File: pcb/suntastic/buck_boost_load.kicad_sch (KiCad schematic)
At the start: 2 parts, among them J5 Vin_TO_buck_boost, J6 Vout_FROM_buck_boost

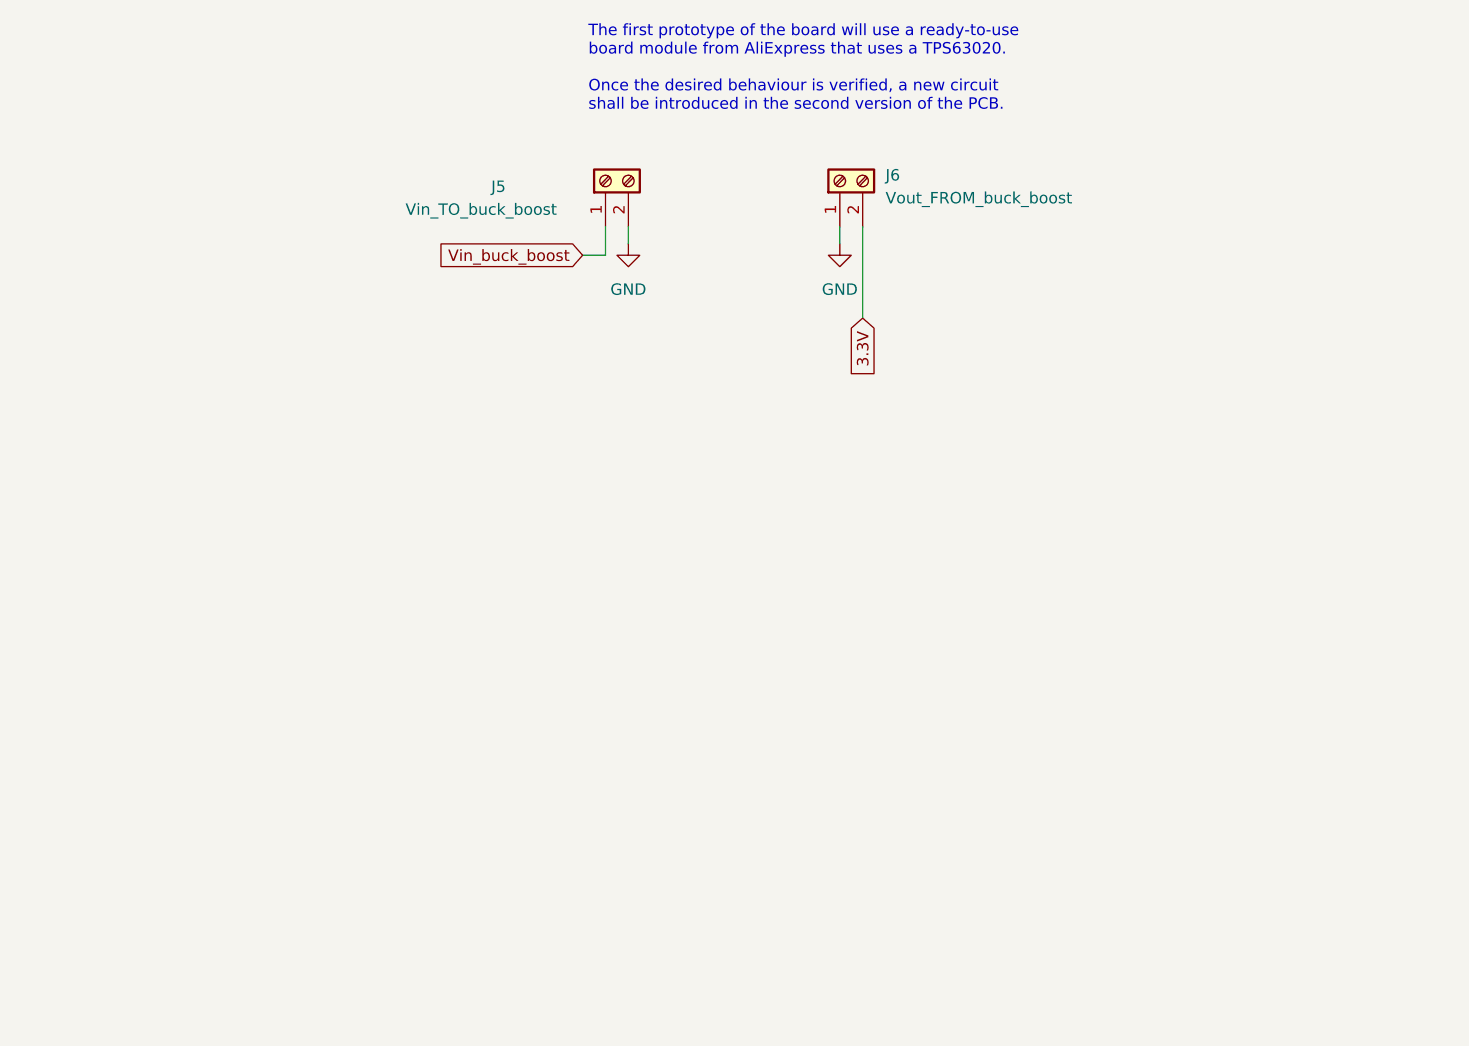
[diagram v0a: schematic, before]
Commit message: Add two alternatives to obtain 3.3V for the SX chip
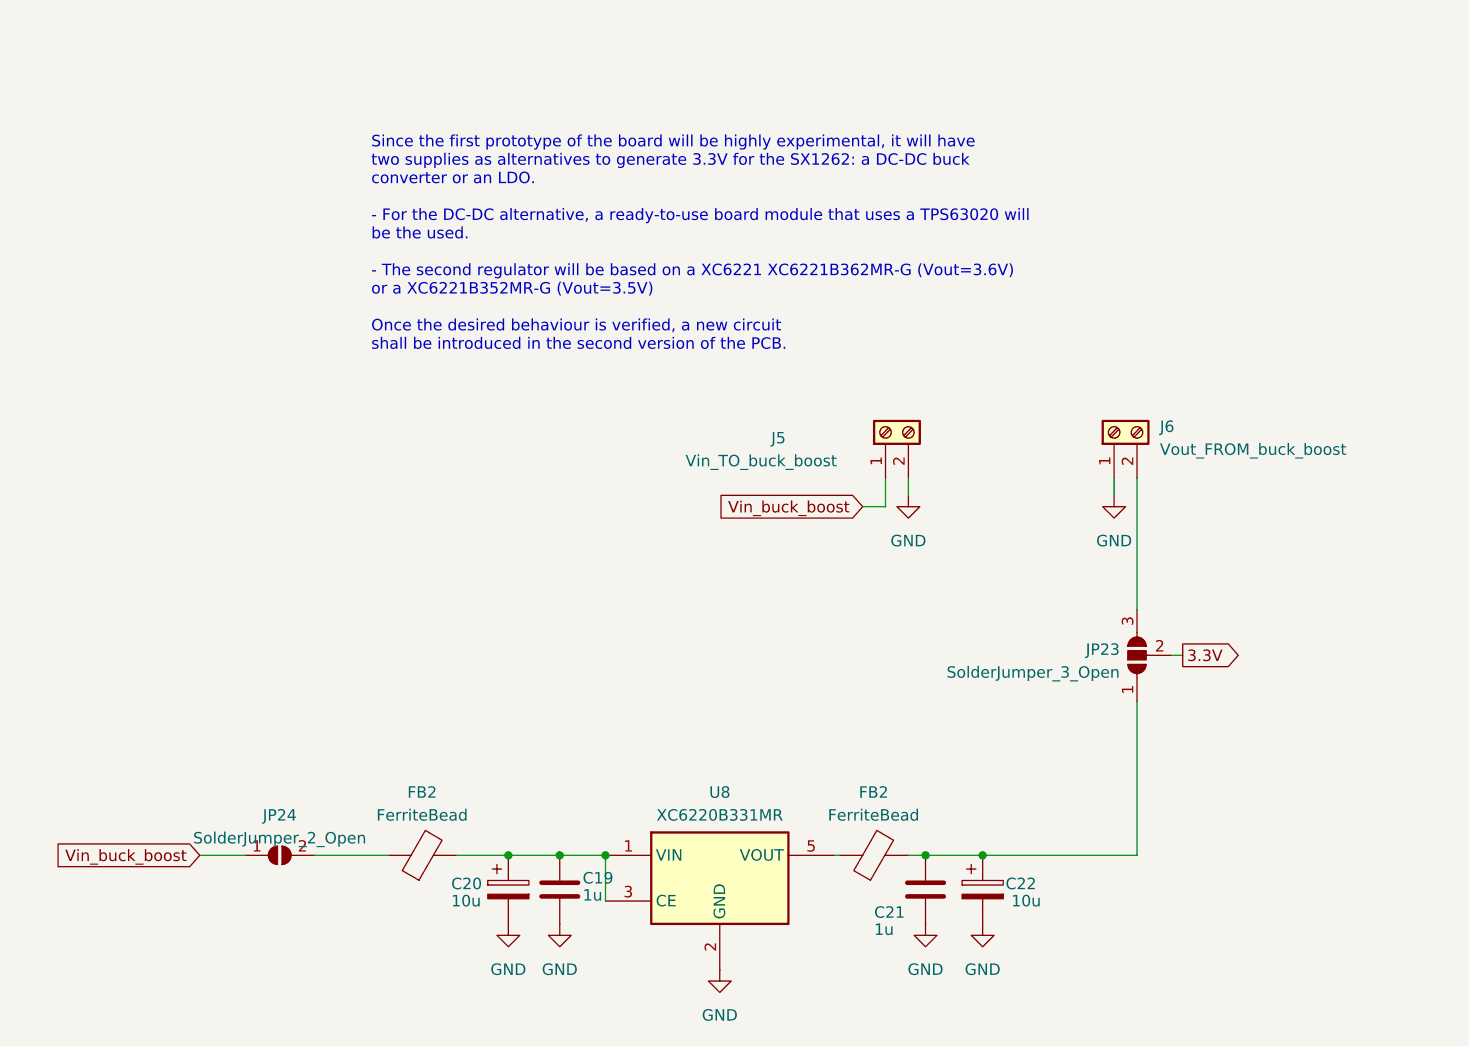
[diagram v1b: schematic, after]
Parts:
- added C19, C21: 1u, symbol Device:C
- added C20, C22: 10u, symbol Device:C_Polarized
- added FB2 (x2): FerriteBead, symbol Device:FerriteBead
- added JP23: SolderJumper_3_Open, symbol Jumper:SolderJumper_3_Open
- added JP24: SolderJumper_2_Open, symbol Jumper:SolderJumper_2_Open
- added U8: XC6220B331MR, Package_TO_SOT_SMD:SOT-23-5_HandSoldering, symbol Regulator_Linear:XC6220B331MR
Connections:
- net 3.3V: now also JP23.2 (C); no longer J6.2 (Pin_2)
- net GND: now also C19.2, C20.2, C21.2, C22.2, U8.2 (GND)
- net Vin_buck_boost: now also JP24.1 (A)
- new net: FB2.1, U8.5 (VOUT)
- new net: C21.1, C22.1, FB2.2, JP23.1 (A)
- new net: C19.1, C20.1, FB2.2, U8.1 (VIN), U8.3 (CE)
- new net: J6.2 (Pin_2), JP23.3 (B)
- new net: FB2.1, JP24.2 (B)
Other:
- note added: "Since the first prototype of the board will be highly experimental, it will have two supplies as alternatives to generate 3.3V for the SX1262: a DC-DC buck converter or an LDO. - For the DC-DC alternative, a ready-to-use board module that uses a TPS63020 will be the used. - The second regulator will be based on a XC6221 XC6221B362MR-G (Vout=3.6V) or a XC6221B352MR-G (Vout=3.5V) Once the desired b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"
- note removed: "The first prototype of the board will use a ready-to-use board module from AliExpress that uses a TPS63020. Once the desired behaviour is verified, a new circuit shall be introduced in the second version of the PCB."
- moved on the sheet: J5, J6

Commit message: Update footprints
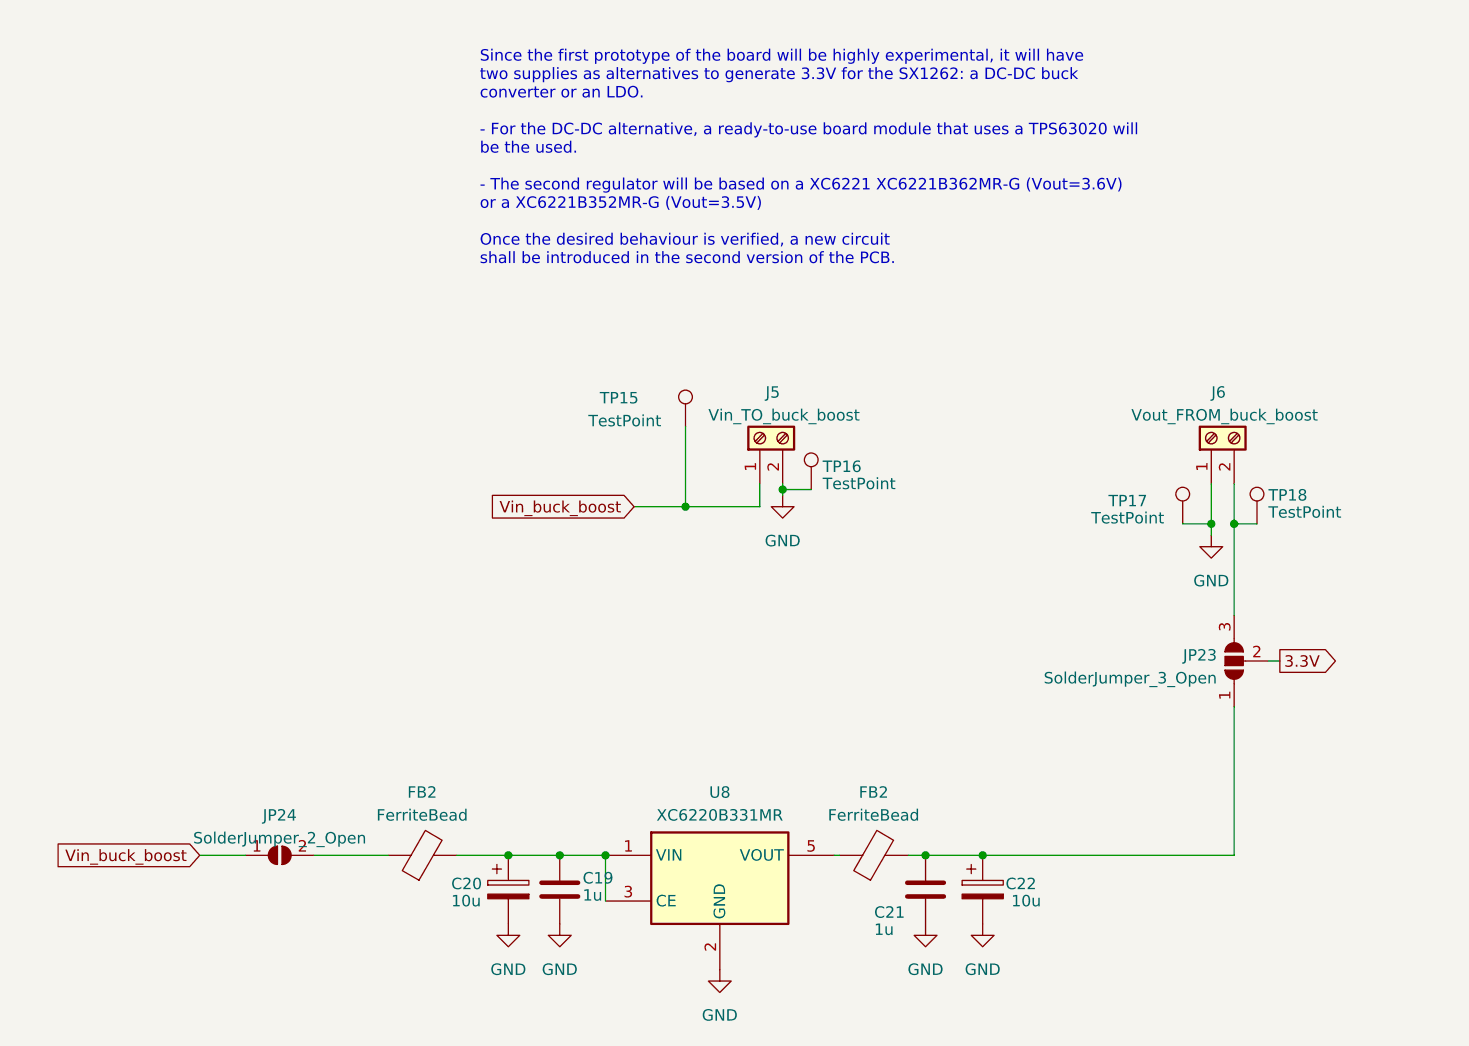
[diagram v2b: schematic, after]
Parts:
- added TP15, TP16, TP17, TP18: TestPoint, TestPoint:TestPoint_THTPad_4.0x4.0mm_Drill2.0mm, symbol Connector:TestPoint
- JP23: footprint (none) -> Jumper:SolderJumper-3_P1.3mm_Open_RoundedPad1.0x1.5mm_NumberLabels
- JP24: footprint (none) -> Jumper:SolderJumper-2_P1.3mm_Open_RoundedPad1.0x1.5mm
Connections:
- net GND: now also TP16.1, TP17.1
- net Vin_buck_boost: now also TP15.1
- net at J6.2 (Pin_2), JP23.3 (B): now also TP18.1
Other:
- moved on the sheet: J5, J6, JP23

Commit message: Update more footprints and start with PCB
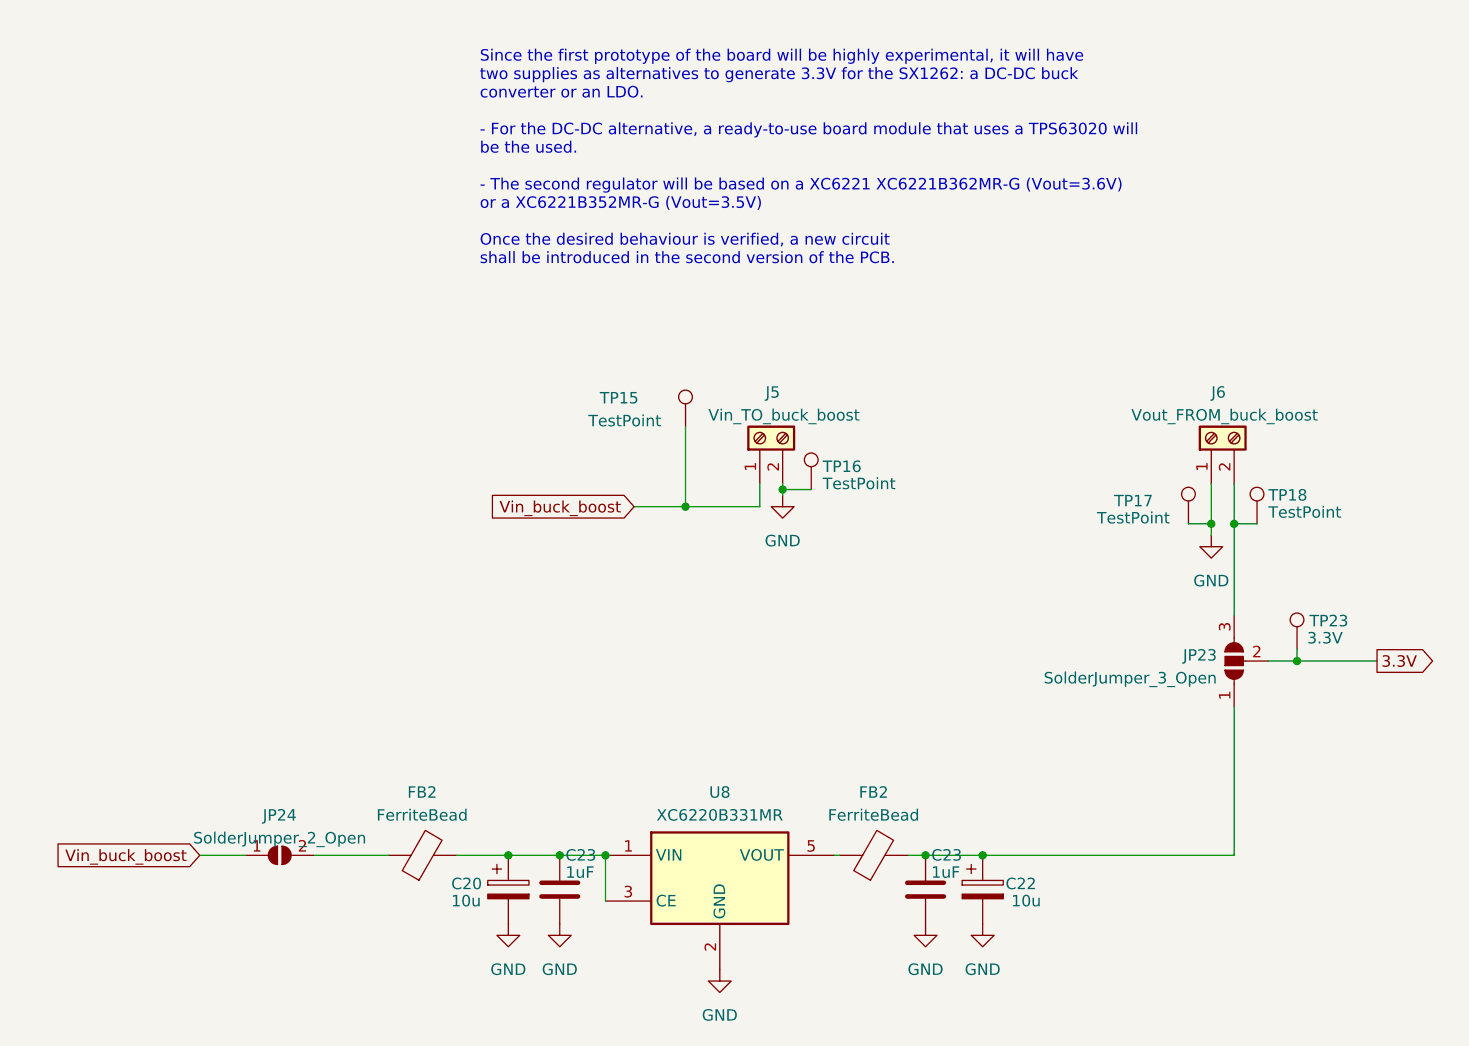
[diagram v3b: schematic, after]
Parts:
- removed C19, C21: 1u, symbol Device:C
- added C23 (x2): 1uF, Capacitor_SMD:C_0603_1608Metric_Pad1.08x0.95mm_HandSolder, symbol Device:C
- added TP23: 3.3V, TestPoint:TestPoint_Bridge_Pitch5.08mm_Drill1.3mm, symbol Connector:TestPoint
- C20, C22: footprint (none) -> Capacitor_SMD:CP_Elec_4x4.5
- FB2: footprint (none) -> Inductor_SMD:L_0603_1608Metric_Pad1.05x0.95mm_HandSolder
- J5, J6: footprint (none) -> TerminalBlock:TerminalBlock_bornier-2_P5.08mm
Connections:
- net 3.3V: now also TP23.1
- net GND: now also C23.2, C23.2
- net at C22.1, FB2.2, JP23.1 (A): now also C23.1
- net at C20.1, FB2.2, U8.1 (VIN)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: now also C23.1
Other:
- moved on the sheet: TP17
